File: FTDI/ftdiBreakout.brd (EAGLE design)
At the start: 36.5 x 22.9 mm, 8 parts, among them X1 USBSMD

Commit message: added barrel connector and touched up top silk
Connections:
- removed net RXD: U$1.5
- net RXI: now also U$1.5
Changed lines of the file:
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@@
 <wire x1="29.0801" y1="11.2939" x2="27.0885" y2="13.2855" width="0.3048" layer="1"/>
-</signal>
-<signal name="RXD">
-<contactref element="U$1" pad="5"/>
 </signal>
 <signal name="CTS">
@@
 <signal name="RXI">
 <contactref element="JP1" pad="5"/>
+<contactref element="U$1" pad="5"/>
+<wire x1="24.7941" y1="7.0696" x2="27.0885" y2="15.8255" width="0" layer="19" extent="1-1"/>
 </signal>
 </signals>

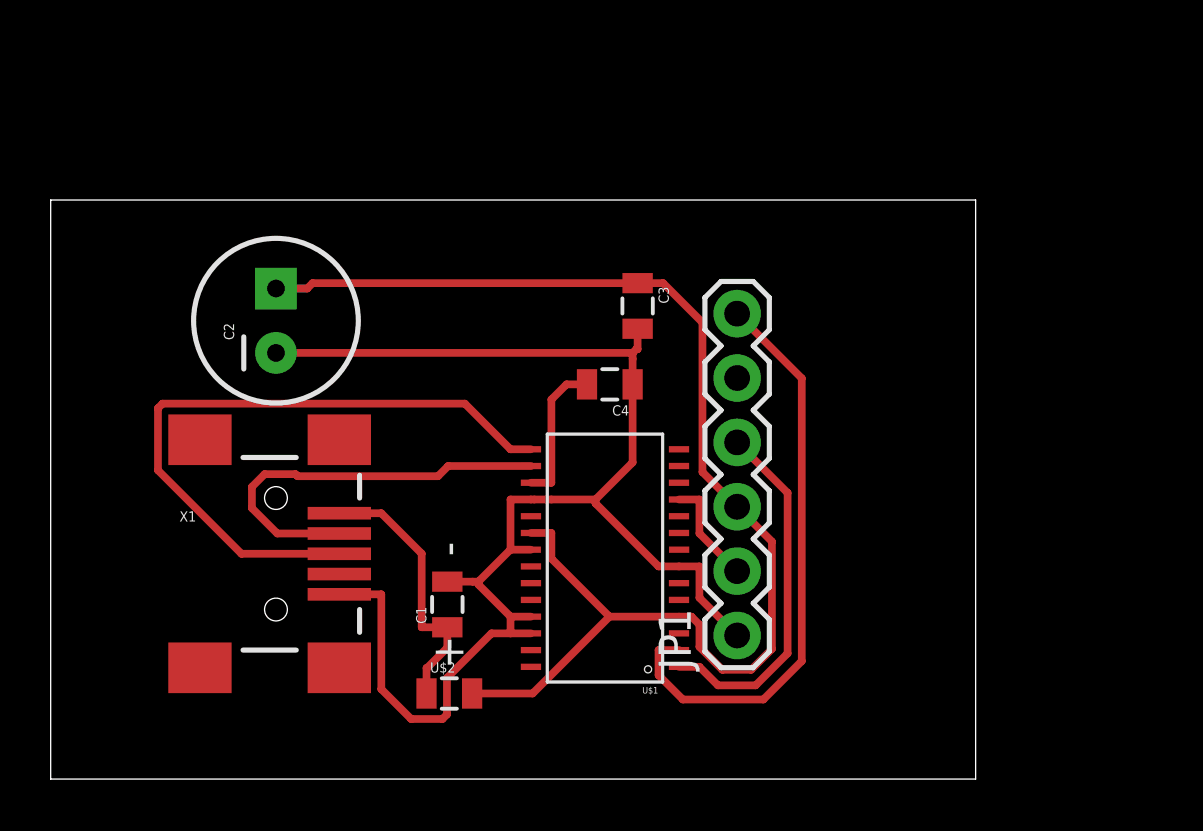
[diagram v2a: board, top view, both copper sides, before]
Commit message: Tested versions of breakout boards
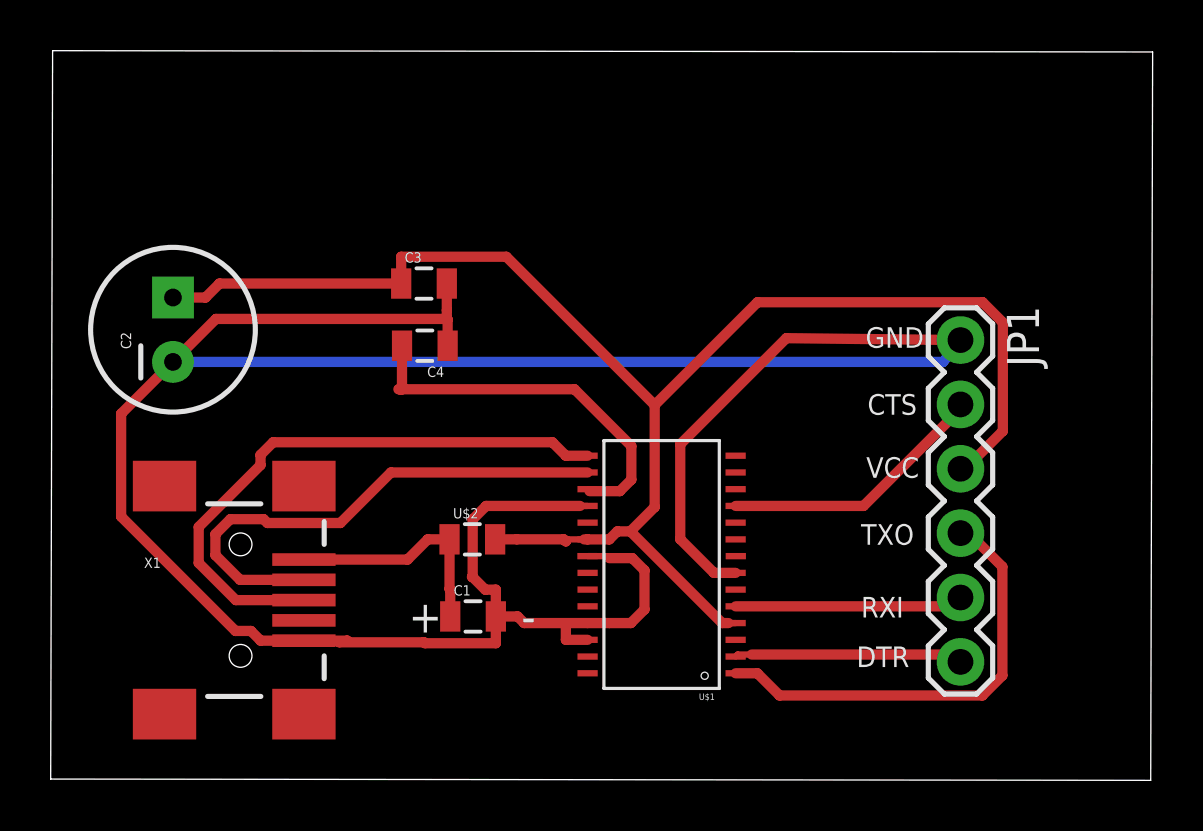
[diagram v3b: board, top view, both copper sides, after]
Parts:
- moved JP1 14.6 mm to (35.9, 17.3), turned to 270 degrees
- moved C3 8.48 mm to (14.7, 19.6), turned to 0 degrees
- moved C4 7.46 mm to (14.8, 17.1)
- moved U$2 6.15 mm to (16.6, 9.46)
- moved C2 4.08 mm to (4.83, 17.7)
- moved X1 2.30 mm to (7.49, 7.06)
- moved U$1 2.25 mm to (24.1, 8.80)
- moved C1 1.12 mm to (16.7, 6.42), turned to 0 degrees
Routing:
- net GND: track 56.7 -> 111.3 mm
- net DTR: track 23.2 -> 9.25 mm
- net N$6: track 5.74 -> 15.1 mm
- net RXI: track 0.00 -> 9.30 mm
- net VCC: track 52.7 -> 61.3 mm
- net CTS: track 4.25 -> 10.8 mm
- net N$4: track 16.1 -> 20.5 mm
- net TXO: track 14.3 -> 17.5 mm
- net N$5: track 26.5 -> 23.4 mm
- net N$1: track 10.8 -> 9.13 mm
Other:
- board size 36.5 x 22.9 mm -> 43.5 x 28.8 mm
- board text added: "CTS"
- board text added: "DTR"
- board text added: "GND"
- board text added: "RXI"
- board text added: "TXO"
- board text added: "VCC"
